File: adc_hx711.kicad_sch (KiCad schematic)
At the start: 21 parts, among them J1 Conn_01x04_Male, J2 Conn_01x02_Male, J3 Conn_01x02_Male, Q1 SS8550, U5 HX711

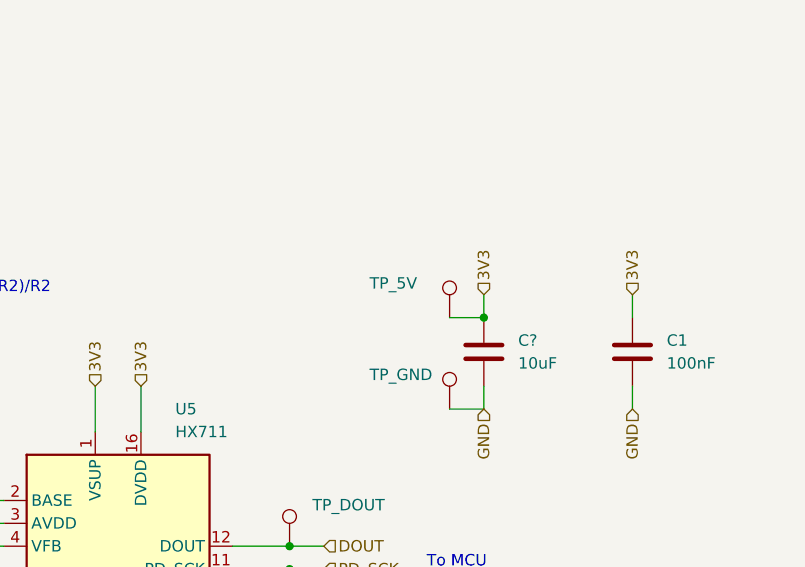
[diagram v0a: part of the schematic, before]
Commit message: added cp2102 schematics
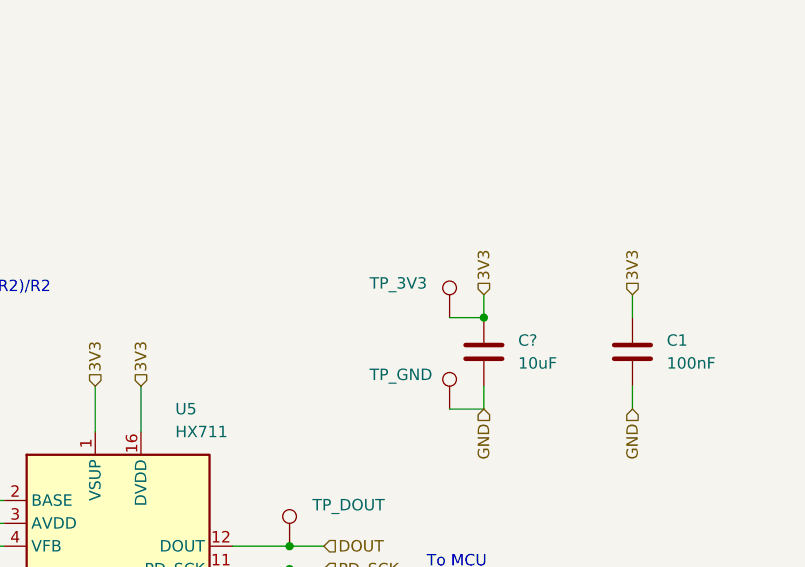
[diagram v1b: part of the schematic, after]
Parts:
- renumbered TP_5V to TP_3V3
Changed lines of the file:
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@@
   (symbol (lib_id "Connector:TestPoint") (at 191.77 60.96 0) (unit 1)
     (in_bom yes) (on_board yes) (dnp no)
-    (property "Reference" "TP_5V" (at 182.88 57.15 0)
+    (property "Reference" "TP_3V3" (at 182.88 57.15 0)
       (effects (font (size 1.27 1.27)) (justify left))
     )
@@
       (project "grip_strength_meter"
         (path "/1f4b217c-5456-4c03-a123-3ef9839449c6/c230759c-e1af-4cfc-a309-bba7f080798c"
-          (reference "TP_5V") (unit 1)
+          (reference "TP_3V3") (unit 1)
         )
       )

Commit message: pre pre production
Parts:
- 3V3: renamed from TP_3V3; footprint (none) -> TestPoint:TestPoint_Pad_1.0x1.0mm
- DOUT1: renamed from TP_DOUT; footprint (none) -> TestPoint:TestPoint_Pad_1.0x1.0mm
- GND1: renamed from TP_GND; footprint (none) -> TestPoint:TestPoint_Pad_1.0x1.0mm
- J1: footprint (none) -> Connector_PinHeader_2.54mm:PinHeader_1x04_P2.54mm_Vertical
- J2, J3: footprint (none) -> Connector_PinHeader_2.54mm:PinHeader_1x02_P2.54mm_Vertical
- L1: footprint (none) -> Inductor_SMD:L_0805_2012Metric
- SCK1: renamed from TP_SCK; footprint (none) -> TestPoint:TestPoint_Pad_1.0x1.0mm
- gave numbers to parts that had none: 5
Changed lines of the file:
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@@
   (symbol (lib_id "Connector:TestPoint") (at 173.99 88.9 180) (unit 1)
     (in_bom yes) (on_board yes) (dnp no)
-    (property "Reference" "TP_SCK" (at 171.45 93.98 0)
+    (property "Reference" "SCK1" (at 171.45 93.98 0)
       (effects (font (size 1.27 1.27)) (justify right))
     )
@@
       (effects (font (size 1.27 1.27)) (justify right) hide)
     )
-    (property "Footprint" "" (at 168.91 88.9 0)
+    (property "Footprint" "TestPoint:TestPoint_Pad_1.0x1.0mm" (at 168.91 88.9 0)
       (effects (font (size 1.27 1.27)) hide)
     )
@@
       (project "grip_strength_meter"
         (path "/1f4b217c-5456-4c03-a123-3ef9839449c6/c230759c-e1af-4cfc-a309-bba7f080798c"
-          (reference "TP_SCK") (unit 1)
+          (reference "SCK1") (unit 1)
         )
       )
@@
       (effects (font (size 1.27 1.27)) hide)
     )
-    (property "Footprint" "" (at 163.83 120.65 0)
+    (property "Footprint" "Connector_PinHeader_2.54mm:PinHeader_1x02_P2.54mm_Vertical" (at 163.83 120.65 0)
       (effects (font (size 1.27 1.27)) hide)
     )
@@
   (symbol (lib_id "Device:C") (at 134.62 113.03 0) (unit 1)
     (in_bom yes) (on_board yes) (dnp no) (fields_autoplaced)
-    (property "Reference" "C?" (at 138.43 111.7599 0)
+    (property "Reference" "C34" (at 138.43 111.7599 0)
       (effects (font (size 1.27 1.27)) (justify left))
     )
@@
       (project "grip_strength_meter"
         (path "/1f4b217c-5456-4c03-a123-3ef9839449c6/c230759c-e1af-4cfc-a309-bba7f080798c"
-          (reference "C?") (unit 1)
+          (reference "C34") (unit 1)
         )
       )
@@
       (effects (font (size 1.27 1.27)) hide)
     )
-    (property "Footprint" "" (at 76.2 104.14 0)
+    (property "Footprint" "Connector_PinHeader_2.54mm:PinHeader_1x02_P2.54mm_Vertical" (at 76.2 104.14 0)
       (effects (font (size 1.27 1.27)) hide)
     )
@@
       (effects (font (size 1.27 1.27)))
     )
-    (property "Footprint" "" (at 111.76 83.82 0)
+    (property "Footprint" "Inductor_SMD:L_0805_2012Metric" (at 111.76 83.82 0)
       (effects (font (size 1.27 1.27)) hide)
     )
@@
   (symbol (lib_id "Device:C") (at 114.3 102.87 0) (unit 1)
     (in_bom yes) (on_board yes) (dnp no) (fields_autoplaced)
-    (property "Reference" "C?" (at 118.11 101.5999 0)
+    (property "Reference" "C33" (at 118.11 101.5999 0)
       (effects (font (size 1.27 1.27)) (justify left))
     )
@@
       (project "grip_strength_meter"
         (path "/1f4b217c-5456-4c03-a123-3ef9839449c6/c230759c-e1af-4cfc-a309-bba7f080798c"
-          (reference "C?") (unit 1)
+          (reference "C33") (unit 1)
         )
       )
@@
       (effects (font (size 1.27 1.27)) hide)
     )
-    (property "Footprint" "" (at 76.2 86.36 0)
+    (property "Footprint" "Connector_PinHeader_2.54mm:PinHeader_1x04_P2.54mm_Vertical" (at 76.2 86.36 0)
       (effects (font (size 1.27 1.27)) hide)
     )
@@
   (symbol (lib_id "Connector:TestPoint") (at 191.77 60.96 0) (unit 1)
     (in_bom yes) (on_board yes) (dnp no)
-    (property "Reference" "TP_3V3" (at 182.88 57.15 0)
+    (property "Reference" "3V3" (at 182.88 57.15 0)
       (effects (font (size 1.27 1.27)) (justify left))
     )
@@
       (effects (font (size 1.27 1.27)) (justify left) hide)
     )
-    (property "Footprint" "" (at 196.85 60.96 0)
+    (property "Footprint" "TestPoint:TestPoint_Pad_1.0x1.0mm" (at 196.85 60.96 0)
       (effects (font (size 1.27 1.27)) hide)
     )
@@
       (project "grip_strength_meter"
         (path "/1f4b217c-5456-4c03-a123-3ef9839449c6/c230759c-e1af-4cfc-a309-bba7f080798c"
-          (reference "TP_3V3") (unit 1)
+          (reference "3V3") (unit 1)
         )
       )
@@
   (symbol (lib_id "Connector:TestPoint") (at 173.99 86.36 0) (unit 1)
     (in_bom yes) (on_board yes) (dnp no) (fields_autoplaced)
-    (property "Reference" "TP_DOUT" (at 176.53 81.7879 0)
+    (property "Reference" "DOUT1" (at 176.53 81.7879 0)
       (effects (font (size 1.27 1.27)) (justify left))
     )
@@
       (effects (font (size 1.27 1.27)) (justify left) hide)
     )
-    (property "Footprint" "" (at 179.07 86.36 0)
+    (property "Footprint" "TestPoint:TestPoint_Pad_1.0x1.0mm" (at 179.07 86.36 0)
       (effects (font (size 1.27 1.27)) hide)
     )
@@
       (project "grip_strength_meter"
         (path "/1f4b217c-5456-4c03-a123-3ef9839449c6/c230759c-e1af-4cfc-a309-bba7f080798c"
-          (reference "TP_DOUT") (unit 1)
+          (reference "DOUT1") (unit 1)
         )
       )
@@
   (symbol (lib_id "Device:C") (at 93.98 87.63 0) (unit 1)
     (in_bom yes) (on_board yes) (dnp no)
-    (property "Reference" "C?" (at 96.52 86.36 0)
+    (property "Reference" "C31" (at 96.52 86.36 0)
       (effects (font (size 1.27 1.27)) (justify left))
     )
@@
       (project "grip_strength_meter"
         (path "/1f4b217c-5456-4c03-a123-3ef9839449c6/c230759c-e1af-4cfc-a309-bba7f080798c"
-          (reference "C?") (unit 1)
+          (reference "C31") (unit 1)
         )
       )
@@
   (symbol (lib_id "Connector:TestPoint") (at 191.77 71.12 0) (unit 1)
     (in_bom yes) (on_board yes) (dnp no)
-    (property "Reference" "TP_GND" (at 182.88 67.31 0)
+    (property "Reference" "GND1" (at 182.88 67.31 0)
       (effects (font (size 1.27 1.27)) (justify left))
     )
@@
       (effects (font (size 1.27 1.27)) (justify left) hide)
     )
-    (property "Footprint" "" (at 196.85 71.12 0)
+    (property "Footprint" "TestPoint:TestPoint_Pad_1.0x1.0mm" (at 196.85 71.12 0)
       (effects (font (size 1.27 1.27)) hide)
     )
@@
       (project "grip_strength_meter"
         (path "/1f4b217c-5456-4c03-a123-3ef9839449c6/c230759c-e1af-4cfc-a309-bba7f080798c"
-          (reference "TP_GND") (unit 1)
+          (reference "GND1") (unit 1)
         )
       )
@@
   (symbol (lib_id "Device:C") (at 195.58 64.77 0) (unit 1)
     (in_bom yes) (on_board yes) (dnp no) (fields_autoplaced)
-    (property "Reference" "C?" (at 199.39 63.4999 0)
+    (property "Reference" "C35" (at 199.39 63.4999 0)
       (effects (font (size 1.27 1.27)) (justify left))
     )
@@
       (project "grip_strength_meter"
         (path "/1f4b217c-5456-4c03-a123-3ef9839449c6/c230759c-e1af-4cfc-a309-bba7f080798c"
-          (reference "C?") (unit 1)
+          (reference "C35") (unit 1)
         )
       )
@@
   (symbol (lib_id "Device:C") (at 106.68 87.63 0) (unit 1)
     (in_bom yes) (on_board yes) (dnp no)
-    (property "Reference" "C?" (at 109.22 86.36 0)
+    (property "Reference" "C32" (at 109.22 86.36 0)
       (effects (font (size 1.27 1.27)) (justify left))
     )
@@
       (project "grip_strength_meter"
         (path "/1f4b217c-5456-4c03-a123-3ef9839449c6/c230759c-e1af-4cfc-a309-bba7f080798c"
-          (reference "C?") (unit 1)
-        )
-      )
+          (reference "C32") (unit 1)
+        )
+      )
